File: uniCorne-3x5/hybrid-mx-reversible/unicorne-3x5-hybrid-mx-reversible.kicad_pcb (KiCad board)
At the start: 2 copper layers, 114.7 x 91.4 mm, 87 parts, among them J1 MJ-4PP-9, J2 Nice!View, J3 Conn_01x02, J4 Conn_01x03, SW1 SW_MX_HS, SW10 SW_MX_HS, SW11 SW_MX_HS, SW12 SW_MX_HS, SW13 SW_MX_HS, SW14 SW_MX_HS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

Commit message: amended hybrid 3x5
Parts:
- U1: footprint TB2086_MISC:ProMicro-ish-dn-rev-unrouted_3x5 -> TB2086_MISC:ProMicro-ish-dn-rev-unrouted_3x6
- moved R4 1.63 mm to (184.3, 111.8)
- moved R3 1.63 mm to (184.3, 109.9)
- moved JP9 0.88 mm to (188.5, 110.8)
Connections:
- PSW1 pad 1: unconnected-(PSW1-A-Pad1) -> BAT+
- PSW1 pad 3: BAT+ -> unconnected-(PSW1-C-Pad3)
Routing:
- net LED: track 42.8 -> 60.1 mm, vias 3 -> 4
- net unconnected-(U1-RAW-Pad24): track 28.3 -> 11.0 mm
- net SCL: track 59.5 -> 66.1 mm, vias 4 -> 3
- net unconnected-(PSW1-A-Pad1): track 6.66 -> 0.00 mm
- net DATA: track 64.8 -> 70.6 mm
- net unconnected-(PSW1-C-Pad3): track 0.00 -> 5.32 mm
- net GND: track 34.9 -> 38.3 mm
- net row3: track 89.5 -> 86.2 mm
- net row1: track 116.8 -> 120.0 mm, vias 1 -> 2
- net unconnected-(U1-B3-Pad15): track 18.6 -> 16.1 mm
- net row0: track 122.5 -> 124.8 mm, vias 1 -> 2
- net row2: track 131.6 -> 133.8 mm, vias 1 -> 2
- net BAT+: track 16.1 -> 14.2 mm
- net SDA: track 71.4 -> 69.8 mm
- net VCC: track 499.8 -> 501.2 mm, vias 3 -> 4
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
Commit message: amended chocolate 3x5
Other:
- board text added: "uniCorne Hybrid 3x5"
- board text removed: "uniCorne Hybrid"

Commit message: small tweak
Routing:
- net DATA: track 70.6 -> 76.4 mm
- net RESET: track 58.4 -> 62.9 mm
- net Net-(JP9-C): track 16.0 -> 15.4 mm
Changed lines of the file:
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@@
         (effects (font (size 0.75 0.5) (thickness 0.125)) (justify mirror))
     )
-    (fp_text user "GND" (at 3.75 -16.563) (layer "B.SilkS")
+    (fp_text user "GND" (at 3.75 -16.28) (layer "B.SilkS")
         (effects (font (size 0.75 0.5) (thickness 0.125)) (justify mirror))
     )
-    (fp_text user "BAT+" (at -3.3183 -16.575) (layer "B.SilkS")
+    (fp_text user "BAT+" (at -3.3183 -16.292) (layer "B.SilkS")
         (effects (font (size 0.75 0.5) (thickness 0.125)) (justify mirror))
     )
@@
         (effects (font (size 0.75 0.5) (thickness 0.125)))
     )
-    (fp_text user "GND" (at -3.4015 -16.5938) (layer "F.SilkS")
+    (fp_text user "GND" (at -3.4015 -16.3108) (layer "F.SilkS")
         (effects (font (size 0.75 0.5) (thickness 0.125)))
     )
@@
         (effects (font (size 0.75 0.5) (thickness 0.125)))
     )
-    (fp_text user "BAT+" (at 3.5 -16.55) (layer "F.SilkS")
+    (fp_text user "BAT+" (at 3.5 -16.267) (layer "F.SilkS")
         (effects (font (size 0.75 0.5) (thickness 0.125)))
     )
@@
   (segment (start 97.65 77.209996) (end 97.65 78.45) (width 0.25) (layer "F.Cu") (net 2))
   (segment (start 95.834824 75.39482) (end 97.65 77.209996) (width 0.25) (layer "F.Cu") (net 2))
-  (segment (start 188.51 110.68) (end 189.51 110.68) (width 0.25) (layer "F.Cu") (net 3))
-  (segment (start 190.15 113.37) (end 191.35 114.57) (width 0.25) (layer "F.Cu") (net 3))
-  (segment (start 189.51 110.68) (end 190.15 111.32) (width 0.25) (layer "F.Cu") (net 3))
-  (segment (start 190.15 111.32) (end 190.15 113.37) (width 0.25) (layer "F.Cu") (net 3))
-  (segment (start 189.63 110.8) (end 190.15 111.32) (width 0.25) (layer "B.Cu") (net 3))
-  (segment (start 188.51 110.68) (end 188.63 110.8) (width 0.25) (layer "B.Cu") (net 3))
-  (segment (start 190.15 111.32) (end 190.15 113.37) (width 0.25) (layer "B.Cu") (net 3))
+  (segment (start 189.85 111.34) (end 189.85 113.07) (width 0.25) (layer "F.Cu") (net 3))
+  (segment (start 188.51 110.68) (end 189.19 110.68) (width 0.25) (layer "F.Cu") (net 3))
+  (segment (start 189.19 110.68) (end 189.85 111.34) (width 0.25) (layer "F.Cu") (net 3))
+  (segment (start 189.85 113.07) (end 191.35 114.57) (width 0.25) (layer "F.Cu") (net 3))
+  (segment (start 189.31 110.8) (end 189.85 111.34) (width 0.25) (layer "B.Cu") (net 3))
+  (segment (start 188.63 110.8) (end 189.31 110.8) (width 0.25) (layer "B.Cu") (net 3))
+  (segment (start 189.85 113.07) (end 191.35 114.57) (width 0.25) (layer "B.Cu") (net 3))
   (segment (start 192 119.87) (end 192 115.22) (width 0.25) (layer "B.Cu") (net 3))
-  (segment (start 190.15 113.37) (end 191.35 114.57) (width 0.25) (layer "B.Cu") (net 3))
-  (segment (start 188.63 110.8) (end 189.63 110.8) (width 0.25) (layer "B.Cu") (net 3))
+  (segment (start 189.85 111.34) (end 189.85 113.07) (width 0.25) (layer "B.Cu") (net 3))
   (segment (start 180.6264 75.6864) (end 180.6264 74.7992) (width 0.25) (layer "F.Cu") (net 4))
   (segment (start 183.94 83.437268) (end 182.89 82.387268) (width 0.25) (layer "F.Cu") (net 4))
@@
   (via (at 188.5 109.29) (size 0.6) (drill 0.4) (layers "F.Cu" "B.Cu") (net 4))
   (via (at 189.91 76.17) (size 0.6) (drill 0.4) (layers "F.Cu" "B.Cu") (net 4))
-  (segment (start 191.5034 73.5742) (end 193.579812 73.5742) (width 0.25) (layer "B.Cu") (net 4))
+  (segment (start 193.83 113.25) (end 190.75 113.25) (width 0.25) (layer "B.Cu") (net 4))
   (segment (start 190.2784 74.7992) (end 191.5034 73.5742) (width 0.25) (layer "B.Cu") (net 4))
+  (segment (start 190.3 112.8) (end 190.3 111.153604) (width 0.25) (layer "B.Cu") (net 4))
+  (segment (start 189.78 110.17) (end 188.9 109.29) (width 0.25) (layer "B.Cu") (net 4))
   (segment (start 190.2784 75.8016) (end 190.2784 74.7992) (width 0.25) (layer "B.Cu") (net 4))
-  (segment (start 188.5 109.29) (end 188.42 109.29) (width 0.25) (layer "B.Cu") (net 4))
-  (segment (start 194.43 74.424388) (end 194.43 108.504529) (width 0.25) (layer "B.Cu") (net 4))
+  (segment (start 191.5034 73.5742) (end 193.579812 73.5742) (width 0.25) (layer "B.Cu") (net 4))
+  (segment (start 194.43 74.424388) (end 194.43 112.65) (width 0.25) (layer "B.Cu") (net 4))
+  (segment (start 190.3 111.153604) (end 189.78 110.633604) (width 0.25) (layer "B.Cu") (net 4))
+  (segment (start 189.78 110.633604) (end 189.78 110.17) (width 0.25) (layer "B.Cu") (net 4))
   (segment (start 189.91 76.17) (end 190.2784 75.8016) (width 0.25) (layer "B.Cu") (net 4))
-  (segment (start 188.95 109.82) (end 188.5 109.37) (width 0.25) (layer "B.Cu") (net 4))
-  (segment (start 193.114529 109.82) (end 188.95 109.82) (width 0.25) (layer "B.Cu") (net 4))
-  (segment (start 188.42 109.29) (end 188.51 109.38) (width 0.25) (layer "B.Cu") (net 4))
-  (segment (start 188.5 109.37) (end 188.5 109.29) (width 0.25) (layer "B.Cu") (net 4))
-  (segment (start 194.43 108.504529) (end 193.114529 109.82) (width 0.25) (layer "B.Cu") (net 4))
+  (segment (start 194.43 112.65) (end 193.83 113.25) (width 0.25) (layer "B.Cu") (net 4))
   (segment (start 193.579812 73.5742) (end 194.43 74.424388) (width 0.25) (layer "B.Cu") (net 4))
+  (segment (start 190.75 113.25) (end 190.3 112.8) (width 0.25) (layer "B.Cu") (net 4))
   (segment (start 180.05 79.3028) (end 180.6264 79.8792) (width 0.5) (layer "F.Cu") (net 5))
   (segment (start 191.15 75.7) (end 190.2784 74.8284) (width 0.5) (layer "F.Cu") (net 5))
@@
   (segment (start 180.6264 95.1192) (end 180.6264 94.0336) (width 0.25) (layer "B.Cu") (net 33))
   (segment (start 183.49 84.280584) (end 183.659416 84.45) (width 0.25) (layer "F.Cu") (net 34))
-  (segment (start 193.489812 78.5642) (end 194.46 79.534388) (width 0.25) (layer "F.Cu") (net 34))
+  (segment (start 190.2784 77.3392) (end 191.5034 78.5642) (width 0.25) (layer "F.Cu") (net 34))
+  (segment (start 191.58 112.75) (end 191.58 112.075) (width 0.25) (layer "F.Cu") (net 34))
+  (segment (start 191.5034 78.5642) (end 193.489812 78.5642) (width 0.25) (layer "F.Cu") (net 34))
   (segment (start 189.8034 79.541028) (end 189.8034 79.0542) (width 0.25) (layer "F.Cu") (net 34))
   (segment (start 188.03 84.308463) (end 188.03 83.019772) (width 0.25) (layer "F.Cu") (net 34))
   (segment (start 180.7995 78.57) (end 181.25 79.0205) (width 0.25) (layer "F.Cu") (net 34))
   (segment (start 189.025 82.024772) (end 189.025 80.319428) (width 0.25) (layer "F.Cu") (net 34))
+  (segment (start 193.489812 78.5642) (end 194.46 79.534388) (width 0.25) (layer "F.Cu") (net 34))
   (segment (start 187.888463 84.45) (end 188.03 84.308463) (width 0.25) (layer "F.Cu") (net 34))
   (segment (start 188.03 83.019772) (end 189.025 82.024772) (width 0.25) (layer "F.Cu") (net 34))
+  (segment (start 192.1 113.27) (end 191.58 112.75) (width 0.25) (layer "F.Cu") (net 34))
   (segment (start 183.49 83.623664) (end 183.49 84.280584) (width 0.25) (layer "F.Cu") (net 34))
-  (segment (start 194.46 79.534388) (end 194.46 108.67) (width 0.25) (layer "F.Cu") (net 34))
-  (segment (start 190.2784 77.3392) (end 191.5034 78.5642) (width 0.25) (layer "F.Cu") (net 34))
-  (segment (start 191.5034 78.5642) (end 193.489812 78.5642) (width 0.25) (layer "F.Cu") (net 34))
+  (segment (start 193.81 113.27) (end 192.1 113.27) (width 0.25) (layer "F.Cu") (net 34))
   (segment (start 189.025 80.319428) (end 189.8034 79.541028) (width 0.25) (layer "F.Cu") (net 34))
   (segment (start 181.25 79.0205) (end 181.25 79.68) (width 0.25) (layer "F.Cu") (net 34))
   (segment (start 189.8034 79.0542) (end 190.3 78.5576) (width 0.25) (layer "F.Cu") (net 34))
-  (segment (start 194.46 108.67) (end 191.9875 111.1425) (width 0.25) (layer "F.Cu") (net 34))
   (segment (start 190.3 78.5576) (end 190.3 77.3608) (width 0.25) (layer "F.Cu") (net 34))
+  (segment (start 194.46 79.534388) (end 194.46 112.62) (width 0.25) (layer "F.Cu") (net 34))
   (segment (start 181.25 79.68) (end 182.44 80.87) (width 0.25) (layer "F.Cu") (net 34))
   (segment (start 182.44 82.573664) (end 183.49 83.623664) (width 0.25) (layer "F.Cu") (net 34))
   (segment (start 182.44 80.87) (end 182.44 82.573664) (width 0.25) (layer "F.Cu") (net 34))
   (segment (start 183.659416 84.45) (end 187.888463 84.45) (width 0.25) (layer "F.Cu") (net 34))
+  (segment (start 194.46 112.62) (end 193.81 113.27) (width 0.25) (layer "F.Cu") (net 34))
   (via (at 180.7995 78.57) (size 0.6) (drill 0.4) (layers "F.Cu" "B.Cu") (net 34))
   (segment (start 180.6264 78.3969) (end 180.7995 78.57) (width 0.25) (layer "B.Cu") (net 34))

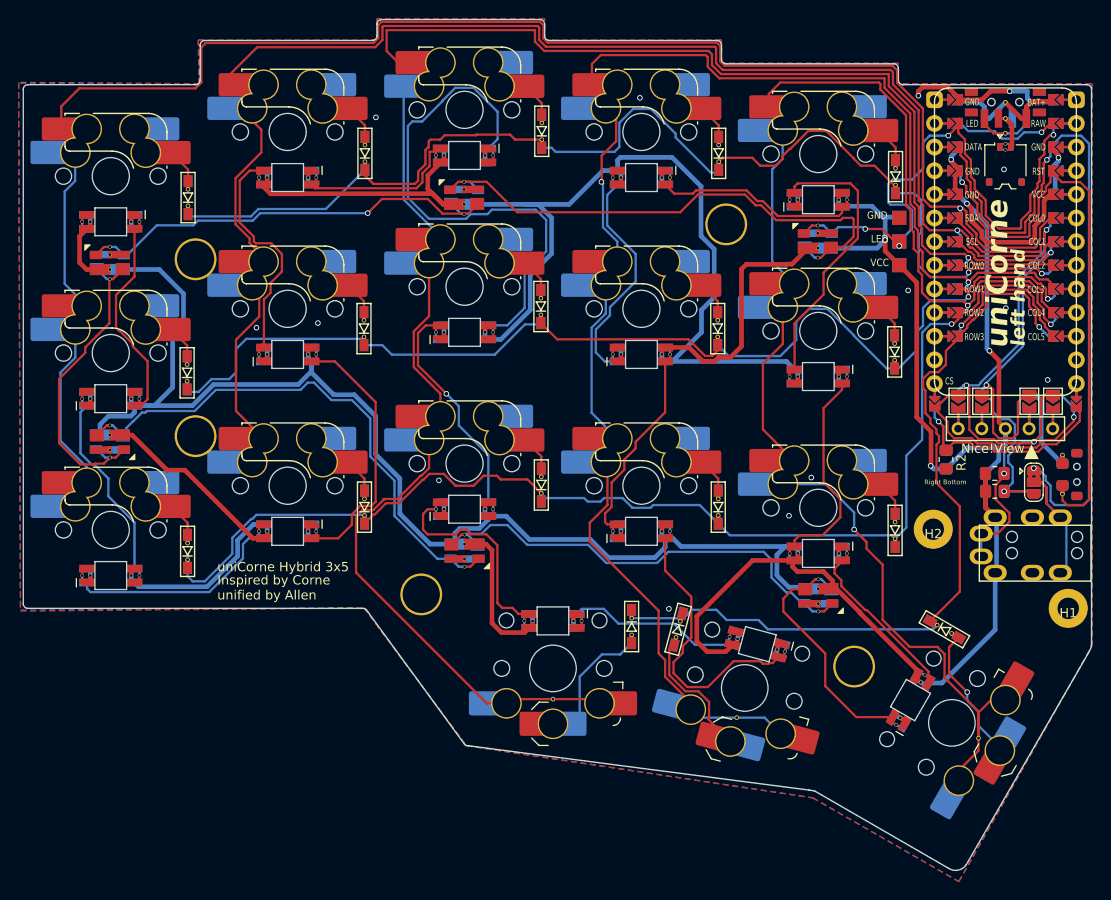
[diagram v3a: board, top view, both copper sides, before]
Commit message: amended footprint for LED
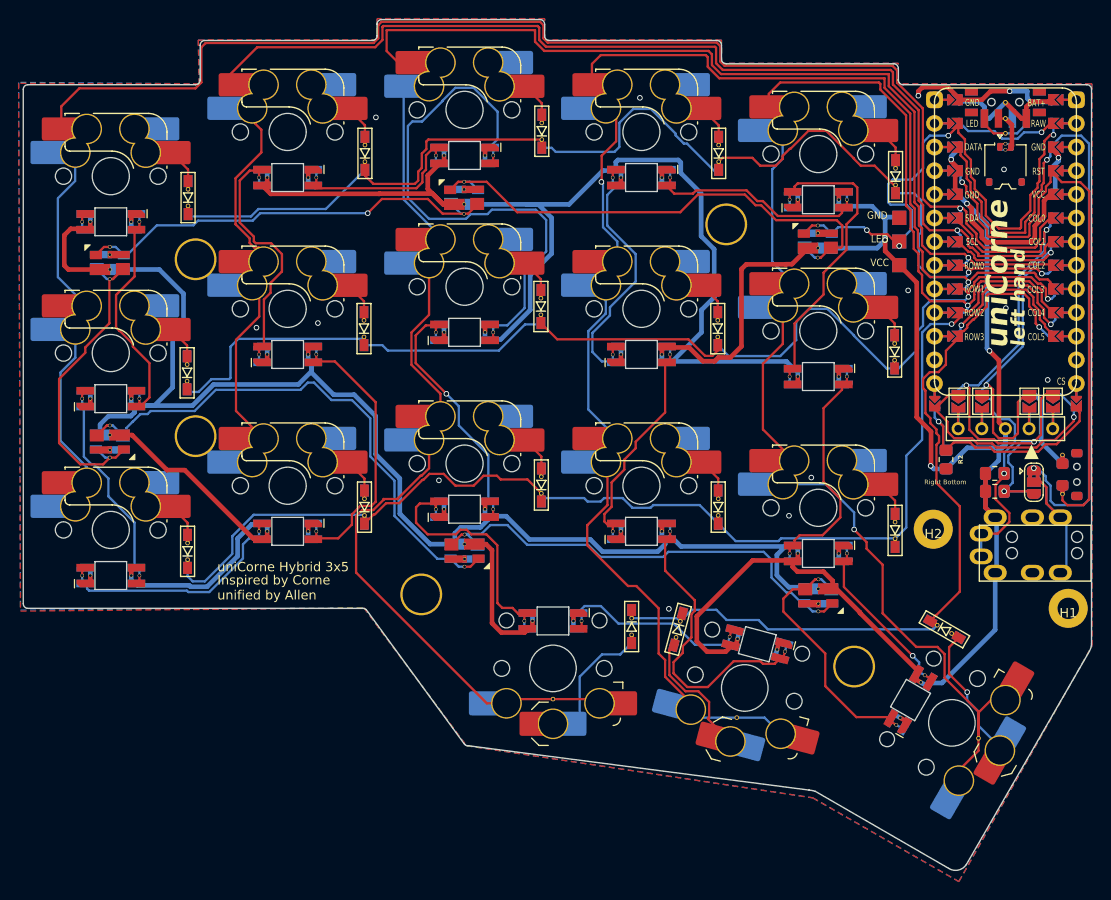
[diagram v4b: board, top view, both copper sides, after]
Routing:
- net Net-(L15-DIN): track 17.7 -> 15.2 mm, vias 0 -> 1
- net Net-(L20-DIN): track 57.5 -> 55.1 mm
- net Net-(L13-DIN): track 22.6 -> 24.7 mm
- net col3: track 151.1 -> 152.1 mm
- net Net-(L11-DOUT): track 20.4 -> 19.6 mm
- net col0: track 173.4 -> 174.0 mm
- net Net-(L23-DOUT): track 50.0 -> 49.4 mm

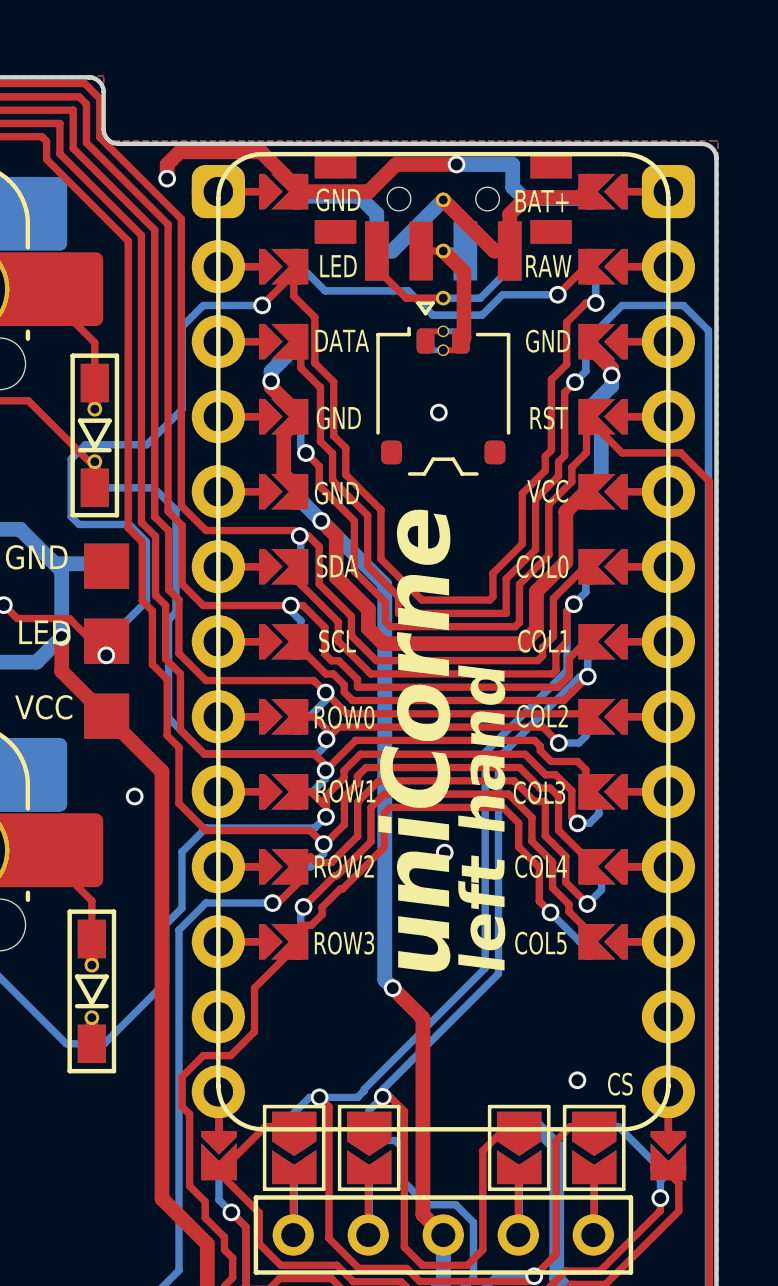
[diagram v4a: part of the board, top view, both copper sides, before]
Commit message: fixed footprint for promicro-ish 3x6
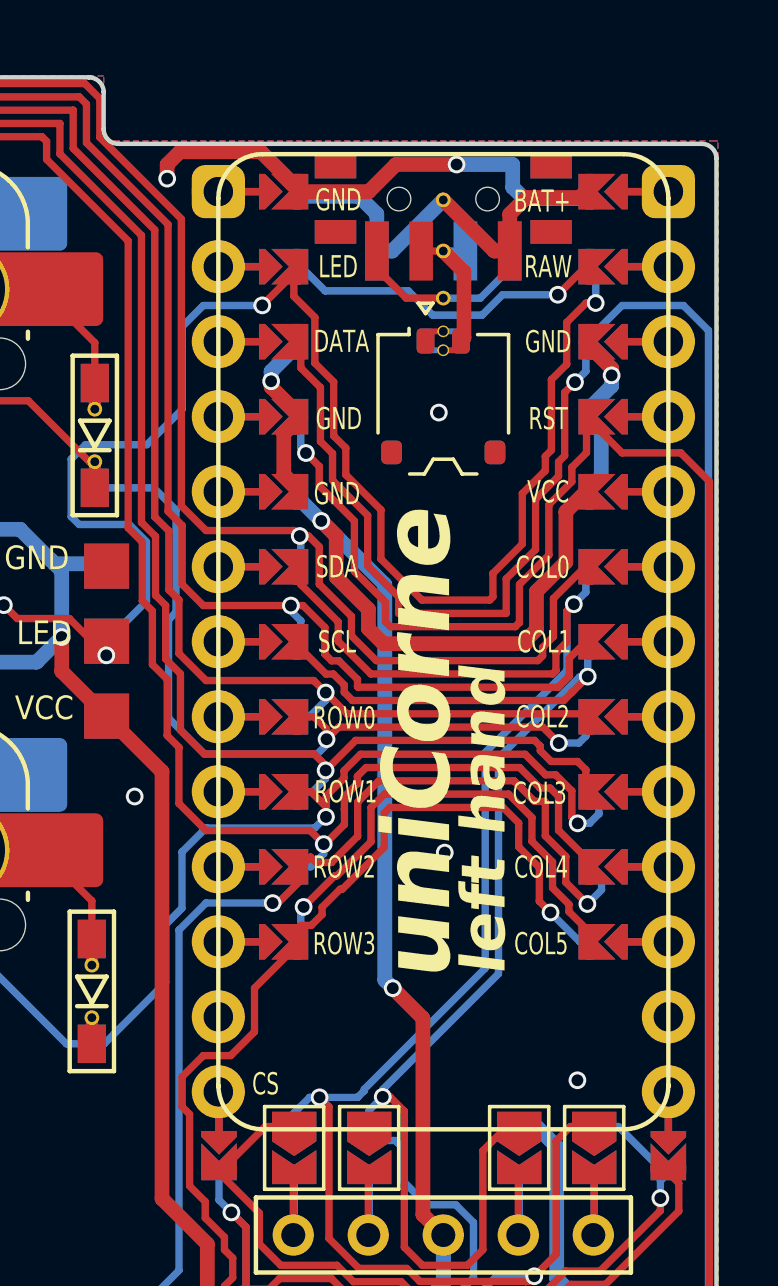
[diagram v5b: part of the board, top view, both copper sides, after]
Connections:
- U1 pad 12: IS_LEFT -> CS
- U1 pad 13: CS -> IS_LEFT
